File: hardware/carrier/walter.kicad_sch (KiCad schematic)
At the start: 22 parts, among them M1 Walter

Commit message: Manually review and fix carrier board schematic
The initial product of clause was mostly okay electrically
but impossible to read. This is a fully redone version
that has all circuits reverified with some modifications.
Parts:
- removed H1, H2, H3, H4: M2, MountingHole:MountingHole_2.2mm_M2, symbol Mechanical:MountingHole
- removed TP1, TP2: GND, TestPoint:TestPoint_Pad_1.0x1.0mm, symbol Connector:TestPoint
- removed TP10: ESP_EN, TestPoint:TestPoint_Pad_1.0x1.0mm, symbol Connector:TestPoint
- removed TP3: SYS, TestPoint:TestPoint_Pad_1.0x1.0mm, symbol Connector:TestPoint
- removed TP4: SYS_SW, TestPoint:TestPoint_Pad_1.0x1.0mm, symbol Connector:TestPoint
- removed TP5: VBAT, TestPoint:TestPoint_Pad_1.0x1.0mm, symbol Connector:TestPoint
- removed TP6: 3V3, TestPoint:TestPoint_Pad_1.0x1.0mm, symbol Connector:TestPoint
- removed TP7: 3V3_EPD, TestPoint:TestPoint_Pad_1.0x1.0mm, symbol Connector:TestPoint
- removed TP8: ESP_TX0, TestPoint:TestPoint_Pad_1.0x1.0mm, symbol Connector:TestPoint
- removed TP9: ESP_RX0, TestPoint:TestPoint_Pad_1.0x1.0mm, symbol Connector:TestPoint
- added C20, C22, C23: 10uF, Capacitor_SMD:C_0603_1608Metric, symbol Device:C
- added C21, C24, C26, C29, C30, C32: 100nF, Capacitor_SMD:C_0603_1608Metric, symbol Device:C
- added C25, C27: 1uF, Capacitor_SMD:C_0603_1608Metric, symbol Device:C
- added C28, C31: 4.7uF, Capacitor_SMD:C_0603_1608Metric, symbol Device:C
- added J3: PANEL, Connector_JST:JST_SH_SM10B-SRSS-TB_1x10-1MP_P1.00mm_Horizontal, symbol Connector_Generic:Conn_01x10
- added J4: CARDKB, Connector_JST:JST_PH_S4B-PH-SM4-TB_1x04-1MP_P2.00mm_Horizontal, symbol Connector_Generic:Conn_01x04
- added J6: EXT_LED, Connector_JST:JST_SH_SM02B-SRSS-TB_1x02-1MP_P1.00mm_Horizontal, symbol Connector_Generic:Conn_01x02
- added J7: HAPTIC, Connector_JST:JST_SH_SM02B-SRSS-TB_1x02-1MP_P1.00mm_Horizontal, symbol Connector_Generic:Conn_01x02
- added J8: PIEZ, Connector_JST:JST_SH_SM02B-SRSS-TB_1x02-1MP_P1.00mm_Horizontal, symbol Connector_Generic:Conn_01x02
- added JP2: auto-boot, Jumper:SolderJumper-2_P1.3mm_Bridged_RoundedPad1.0x1.5mm, symbol Jumper:SolderJumper_2_Bridged
- added Q3: MMBT3904, Package_TO_SOT_SMD:SOT-23, symbol Transistor_BJT:MMBT3904
- added Q4: AO3400A, Package_TO_SOT_SMD:SOT-23, symbol Transistor_FET:AO3400A
- added Q5: UMH3N, Package_TO_SOT_SMD:SOT-363_SC-70-6, symbol Transistor_BJT:UMH3N
- added R20: 0R, Resistor_SMD:R_0603_1608Metric, symbol Device:R
- added R29, R30, R31, R32: 4.7k, Resistor_SMD:R_0603_1608Metric, symbol Device:R
- added R33: 0R, Resistor_SMD:R_1206_3216Metric, symbol Device:R
- added R34, R43: 1k, Resistor_SMD:R_0603_1608Metric, symbol Device:R
- added R35, R36, R44, R45: 100k, Resistor_SMD:R_0603_1608Metric, symbol Device:R
- added R37: 330R, Resistor_SMD:R_0603_1608Metric, symbol Device:R
- added R38, R39: 220R, Resistor_SMD:R_0603_1608Metric, symbol Device:R
- added R40: 15R, Resistor_SMD:R_0603_1608Metric, symbol Device:R
- added R41: 22.1k, Resistor_SMD:R_0603_1608Metric, symbol Device:R
- added R42: 47.5k, Resistor_SMD:R_0603_1608Metric, symbol Device:R
- added R46, R47, R48: 10k, Resistor_SMD:R_0603_1608Metric, symbol Device:R
- added R49: 1M, Resistor_SMD:R_0603_1608Metric, symbol Device:R
- added SW2: SKQGAFE010, Button_Switch_SMD:SW_SPST_SKQG_WithoutStem, symbol Switch:SW_Push
- added TP11: 3V3_AWK, TestPoint:TestPoint_Pad_1.0x1.0mm, symbol Connector:TestPoint
- added U11: SN74LVC2G126DCUR, Package_SO:VSSOP-8_2.3x2mm_P0.5mm, symbol 74xGxx:74LVC2G126
- added U7: LIS2DW12TR, Package_LGA:LGA-12_2x2mm_P0.5mm, symbol pager-carrier:LIS2DW12TR
- added U8: CP2102N-A02-GQFN24, Package_DFN_QFN:QFN-24-1EP_4x4mm_P0.5mm_EP2.6x2.6mm, symbol Interface_USB:CP2102N-Axx-xQFN24
- added U9: DRV2605LDGSR, Package_SO:TSSOP-10_3x3mm_P0.5mm, symbol pager-carrier:DRV2605LDGSR
- TP7: renamed from TP11; value KBD_PWR_N -> AWK_EN_N
- renumbered TP13 to TP10, TP12 to TP8, TP14 to TP9
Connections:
- net 3V3: now also C20.1, C21.1, C22.1, R20.1, R29.1, R30.1, R36.2, R48.2, U7.10 (VDD_IO), U7.2 (CS), U7.9 (VDD)
- net ACC_INT1: now also U7.12 (INT1)
- net ESP_EN: now also Q5.6 (C1)
- net ESP_RX0: now also R48.1, U11.3
- net ESP_TX0: now also U11.2
- net FL_BTN: now also C24.1, R36.1, SW2.1
- net FL_PWM: now also R34.1
- net GND: now also C20.2, C21.2, C22.2, C23.2, C24.2, C25.2, C26.2, C27.2, C28.2, C29.2, C30.1, C31.1, C32.2, J3.2 (Pin_2), J4.4 (Pin_4), J6.2 (Pin_2), Q3.2 (E), R35.2, R40.2, R42.2, R44.2, R45.2, SW2.2, U11.4 (GND), U7.3 (SDO/SA0), U7.6 (GND), U7.7 (RES), U7.8 (GND), U8.18 (~{CTS}), U8.2 (GND), U8.25 (GND), U9.4 (IN/TRIG), U9.8 (GND)
- net SYS_SW: now also R33.2
- net VBUS_DET: now also U11.1, U11.7
- net 3V3_OUT renamed 3V3_AWK
- net 3V3_AWK: now also C23.1, C25.1, C26.1, J4.3 (Pin_3), R31.1, R32.1, TP11.1, U9.10 (VDD), U9.5 (EN), U9.6 (VDD/NC)
- net ACC_SCL renamed AON_SCL
- net AON_SCL: now also R30.2, U7.1 (SCL/SPC)
- net ACC_SDA renamed AON_SDA
- net AON_SDA: now also R29.2, U7.4 (SDA/SDI/SDO)
- net EPD_BUSY renamed EINK_BUSY
- net EINK_BUSY: now also J3.8 (Pin_8)
- net EPD_CS renamed EINK_CS
- net EINK_CS: now also J3.5 (Pin_5)
- net EPD_DC renamed EINK_DC
- net EINK_DC: now also J3.6 (Pin_6)
- net EPD_ENA renamed PIEZ_N
- net PIEZ_N: now also R39.1
- net EPD_MOSI renamed EINK_MOSI
- net EINK_MOSI: now also J3.4 (Pin_4)
- net EPD_RST renamed EINK_RST
- net EINK_RST: now also J3.7 (Pin_7)
- net EPD_SCK renamed EINK_SCK
- net EINK_SCK: now also J3.3 (Pin_3)
- net HAPTIC_EN renamed PIEZ_P
- net PIEZ_P: now also R38.1
- net KBD_PWR_N renamed AWK_EN_N
- net AWK_EN_N: now also JP2.2 (B)
- net KBD_SCL renamed AWK_SCL
- net AWK_SCL: now also J4.1 (Pin_1), U9.2 (SCL)
- net KBD_SDA renamed AWK_SDA
- net AWK_SDA: now also J4.2 (Pin_2), R31.2, R32.2, U9.3 (SDA)
- net MSG_LED renamed EXT_LED
- net EXT_LED: now also R37.1
- new net: JP2.1 (A), Q5.3 (C2)
- new net: J3.1 (Pin_1), R20.2
- new net: Q5.1 (E1), R44.1, R47.1, U8.19 (~{RTS})
- new net: Q5.5 (B2), R47.2
- new net: Q3.1 (B), Q4.2 (S), R40.1
- new net: Q3.3 (C), Q4.1 (G), R34.2, R35.1
- new net: Q5.2 (B1), R46.2
- new net: J7.1 (Pin_1), U9.7 (OUT+)
- new net: J7.2 (Pin_2), U9.9 (OUT-)
- new net: Q5.4 (E2), R45.1, R46.1, U8.23 (~{DTR})
- new net: R41.2, R42.1, U8.8 (VBUS)
- new net: R43.1, U8.9 (~{RST})
- new net: C27.1, U9.1 (REG)
- new net: J8.2 (Pin_2), R39.2, R49.1
- new net: J8.1 (Pin_1), R38.2, R49.2
- new net: J6.1 (Pin_1), R37.2
- new net BRG_3V3: C30.2, C31.2, C32.1, R43.2, U11.8 (VCC), U8.5 (VIO), U8.6 (VDD)
- new net BRG_RXD: U11.6, U8.20 (RXD)
- new net BRG_TXD: U11.5, U8.21 (TXD)
- new net FL_N: J3.10 (Pin_10), Q4.3 (D)
- new net FL_P: J3.9 (Pin_9), R33.1
- new net USB_DM: U8.4 (D-)
- new net USB_DP: U8.3 (D+)
- new net VBUS: C28.1, C29.1, R41.1, U8.7 (VREGIN)
- no-connect marks 0 -> 13
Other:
- note added: "Accelerometer U7 LIS2DW12 on I2C1 (ACC_*), SA0 low = 0x18 Always on from 3V3 CS high = I2C mode, INT1 -> IO16 (RTC wake)"
- note added: "Auto-reset (Espressif): Q2 DTR->EN, Q3 RTS->IO0. JP1 (closed) in Q3's collector lets auto-boot be disabled reset still works."
- note added: "Buffer to disable the serial when no VBUS U6 SN74LVC2G126: both OE from VBUS_DET. A: ESP_TX0 -> BRG_RXD. B: BRG_TXD -> ESP_RX0. 10k keeps ESP_RX0 high with no cable. U6 VCC is BRG_3V3 (bus-powered). with no cable the buffer is unpowered (Ioff outputs) so no LVC quiescent/float current on the battery."
- note added: "Bulk at Walter VIN (pin 28) 2 x 100uF 0805 + 10uF 0603 within 5 mm of the pin."
- note added: "Bus-powered: VREGIN from VBUS VBUS sense pin via 22.1k/47.5k VDD = internal 3.3 V regulator output VIO tied to VDD, 4.7uF + 100nF per power pin. Program the USB product string with Simplicity Studio XpressConfigurator after assembly."
- note added: "E-ink display. J3 10-pin JST SH cable connecting carrier to panel board. The SSD1680 ZIF, boost/charge-pump cluster, and the front-light 6-pin ZIFs live on a separate panel board. This connects the SPI channel, provides measurement points, and also provides a clamped power for the Front Light. Front Light expects 3 or 4 LEDs from Vf 3.3V to vF 2.8V."
- note added: "External LED Header"
- note added: "External Piezzo Header"
- note added: "Front-light button with wake-edge debounce"
- note added: "Haptic (DNP): DRV2605L on I2C1 (0x5A) OUT+/- to J7"
- note added: "I2C Keyboard (CardKB) header. J4 (Grove order): 1 AWK_SCL, 2 AWK_SDA, 3 3V3_AWK, 4 GND Pull-ups to 3V3_SW so whole unit can be depowered."
- note added: "Place U7 away from J7 and the panel cable; X axis along the tin's long edge; mark orientation on silk."
- note added: "Q2/Q3 are the two halves of one UMH3N (Q2A/Q2B) The Walter already pulls EN up (10k) IO0 has only the ESP32 internal pull-up."
- note added: "Test pads"
- note added: "USB Serial connection"
- note added: "Walter ESP32 connections as represetned by 2x14 header. The module is mounted header-side-up under the carrier."
- note removed: "Bulk at Walter VIN (pin 28): 2 x 100uF 0805 + 10uF 0603, within 5 mm of the pin."
- note removed: "IO0 (pin 4, KBD_PWR_N) is a strap, the keyboard-rail gate and the auto-reset boot target; see usb_serial."
- note removed: "Spare IO1/IO5 go to test pads only (TP_IO1 = ADC1_CH0). IO5 also has a DNP 0R to the charger CE. IO4 (RTC GPIO) = FL_BTN, the front-light button, see peripherals."
- note removed: "Test pads, 1.0 mm, top side."
- note removed: "Walter 2x14 header. Pin names as datasheet rev 1.1 Table 1. The module is mounted header-side-up under the carrier; the footprint is the mirror of the vendor top-mount pattern."
- moved on the sheet: C12, C13, C14, M1, TP10, TP7, TP8, TP9

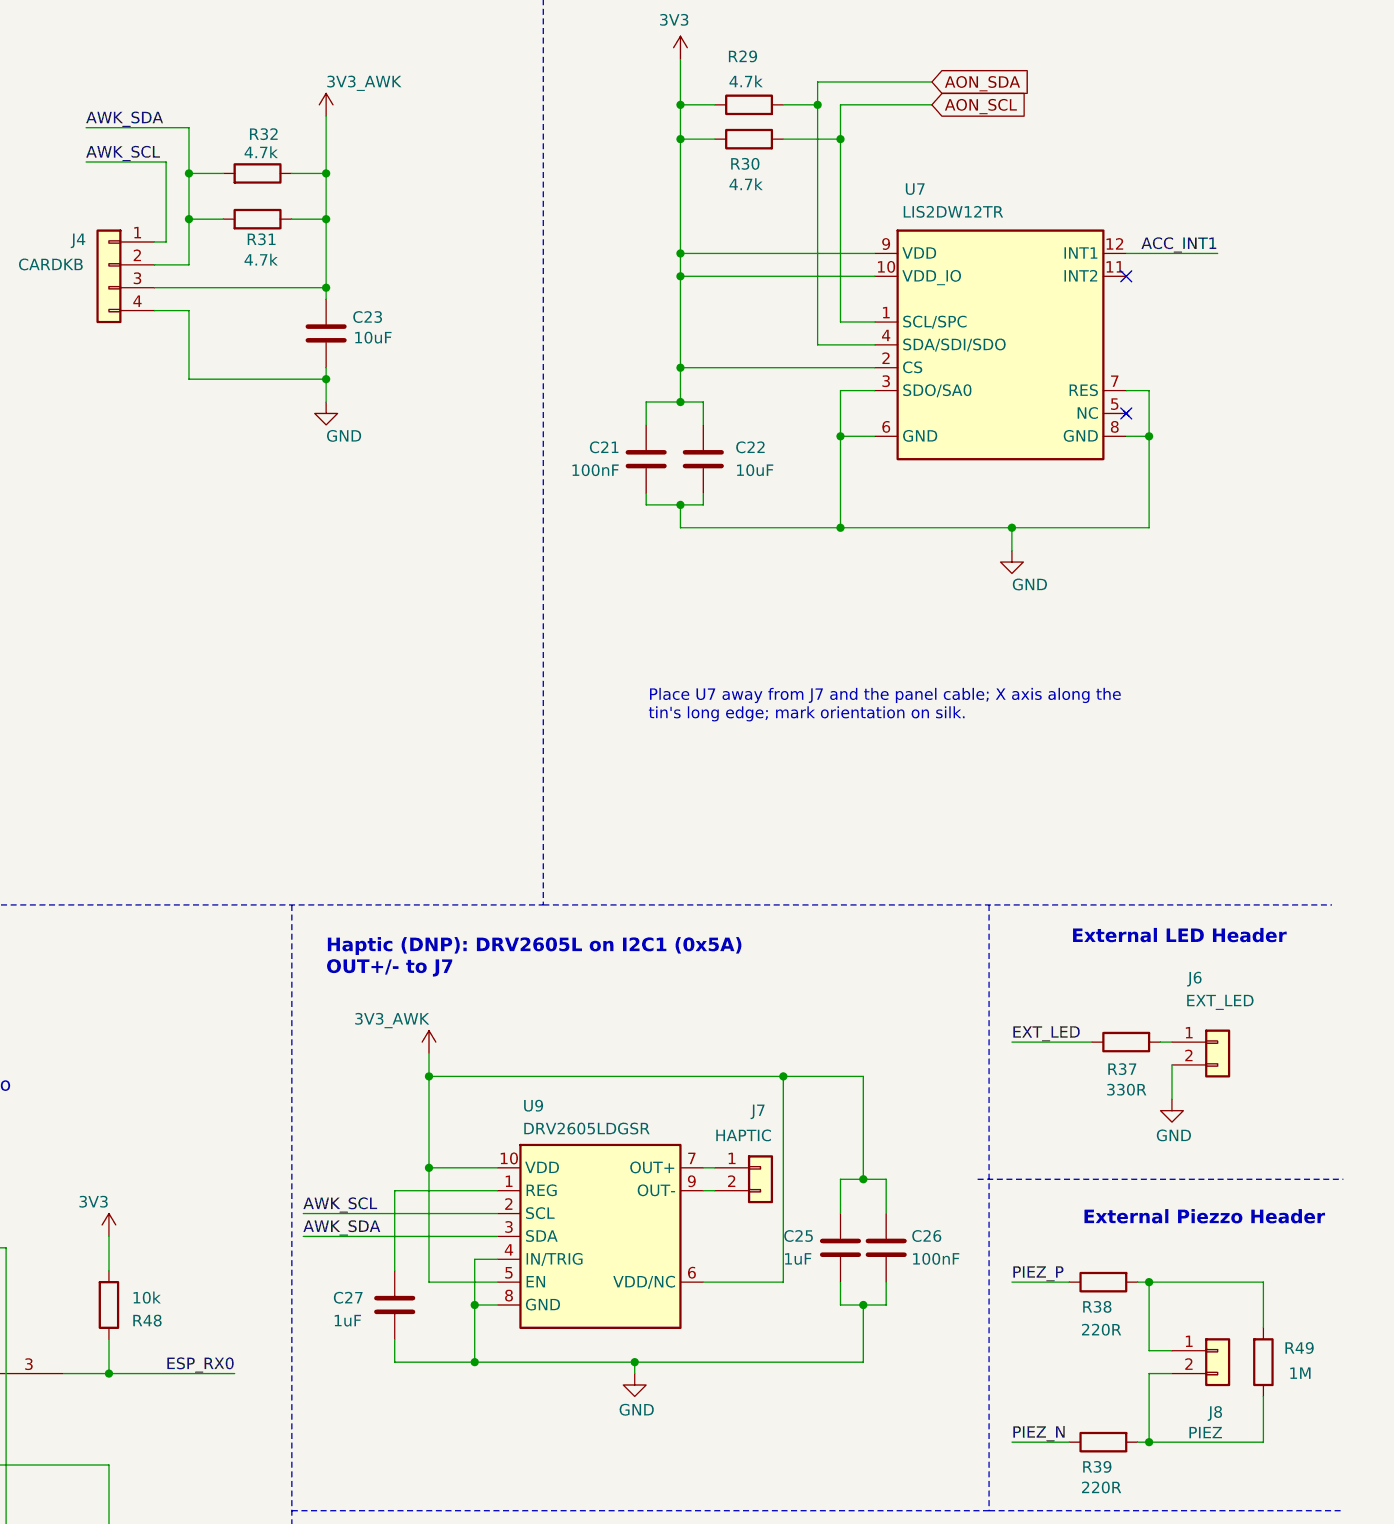
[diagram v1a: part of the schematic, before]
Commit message: Fix some small errors and clean up BOM
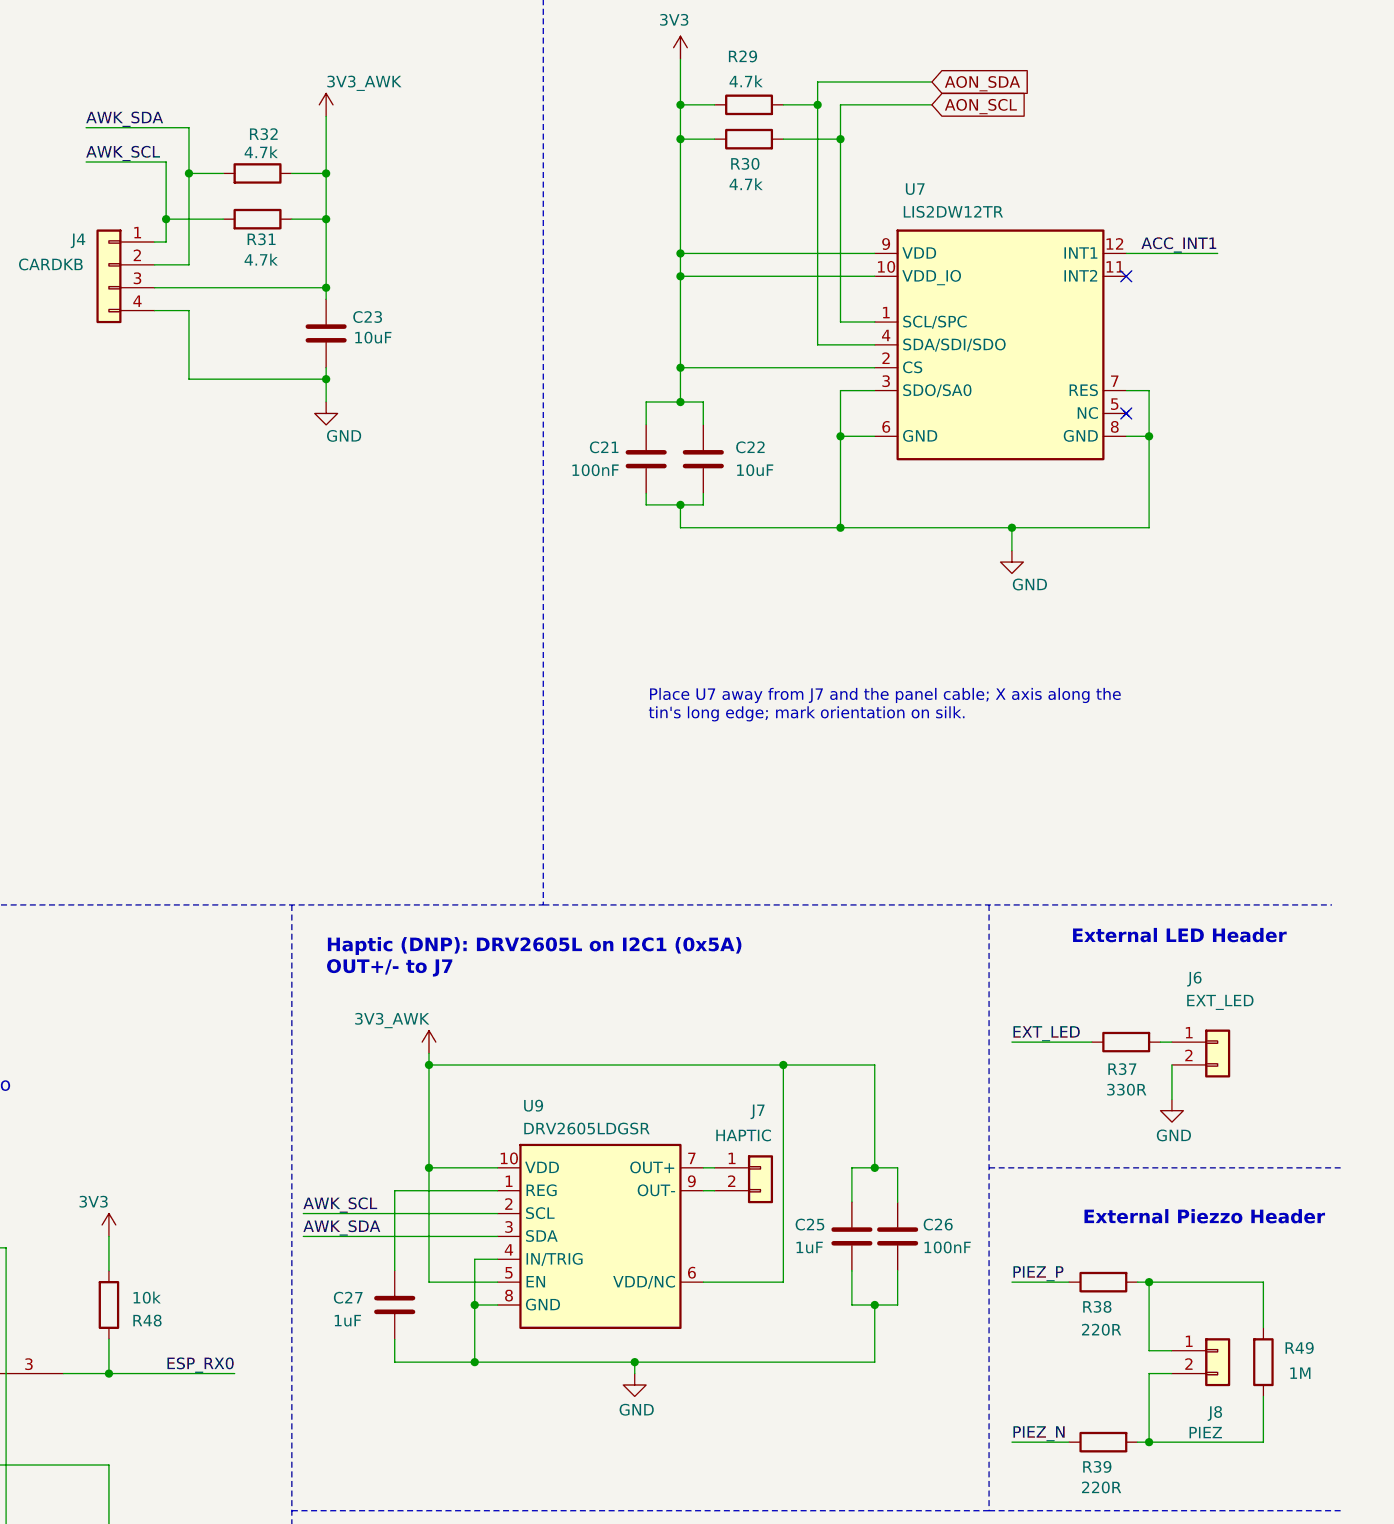
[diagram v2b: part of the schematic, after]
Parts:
- Q3: LCSC (none) -> C20526; MPN (none) -> MMBT3904
- Q4: LCSC C8545 -> C20917; MPN 2N7002 -> AO3400A
- R33: LCSC C18005 -> C17888; MPN 1206W4F330JT5E -> 1206W4F0000T5E; Note R-FL, 1206 for 0.1 W at 50 mA; lower for a brighter light, 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 -> (none)
- R34: LCSC C22775 -> C21190; MPN 0603WAF1000T5E -> 0603WAF1001T5E
- R38, R39: LCSC C23138 -> C22962; MPN 0603WAF3300T5E -> 0603WAF2200T5E
- R40: LCSC C25803 -> C22810; MPN 0603WAF1003T5E -> 0603WAF150JT5E
- R49: LCSC C23138 -> C22935; MPN 0603WAF3300T5E -> 0603WAF1004T5E
- U11: LCSC (none) -> C2652104
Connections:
- net AWK_SCL: now also R31.2
- net AWK_SDA: no longer R31.2
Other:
- moved on the sheet: C25, C26
